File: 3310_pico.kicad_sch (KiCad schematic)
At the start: 37 parts, among them J4 PCDTest, J5 KeypadTest, J6 BuzzerTest, Q1 2N3904, Q2 2N3904, Q3 2N3904

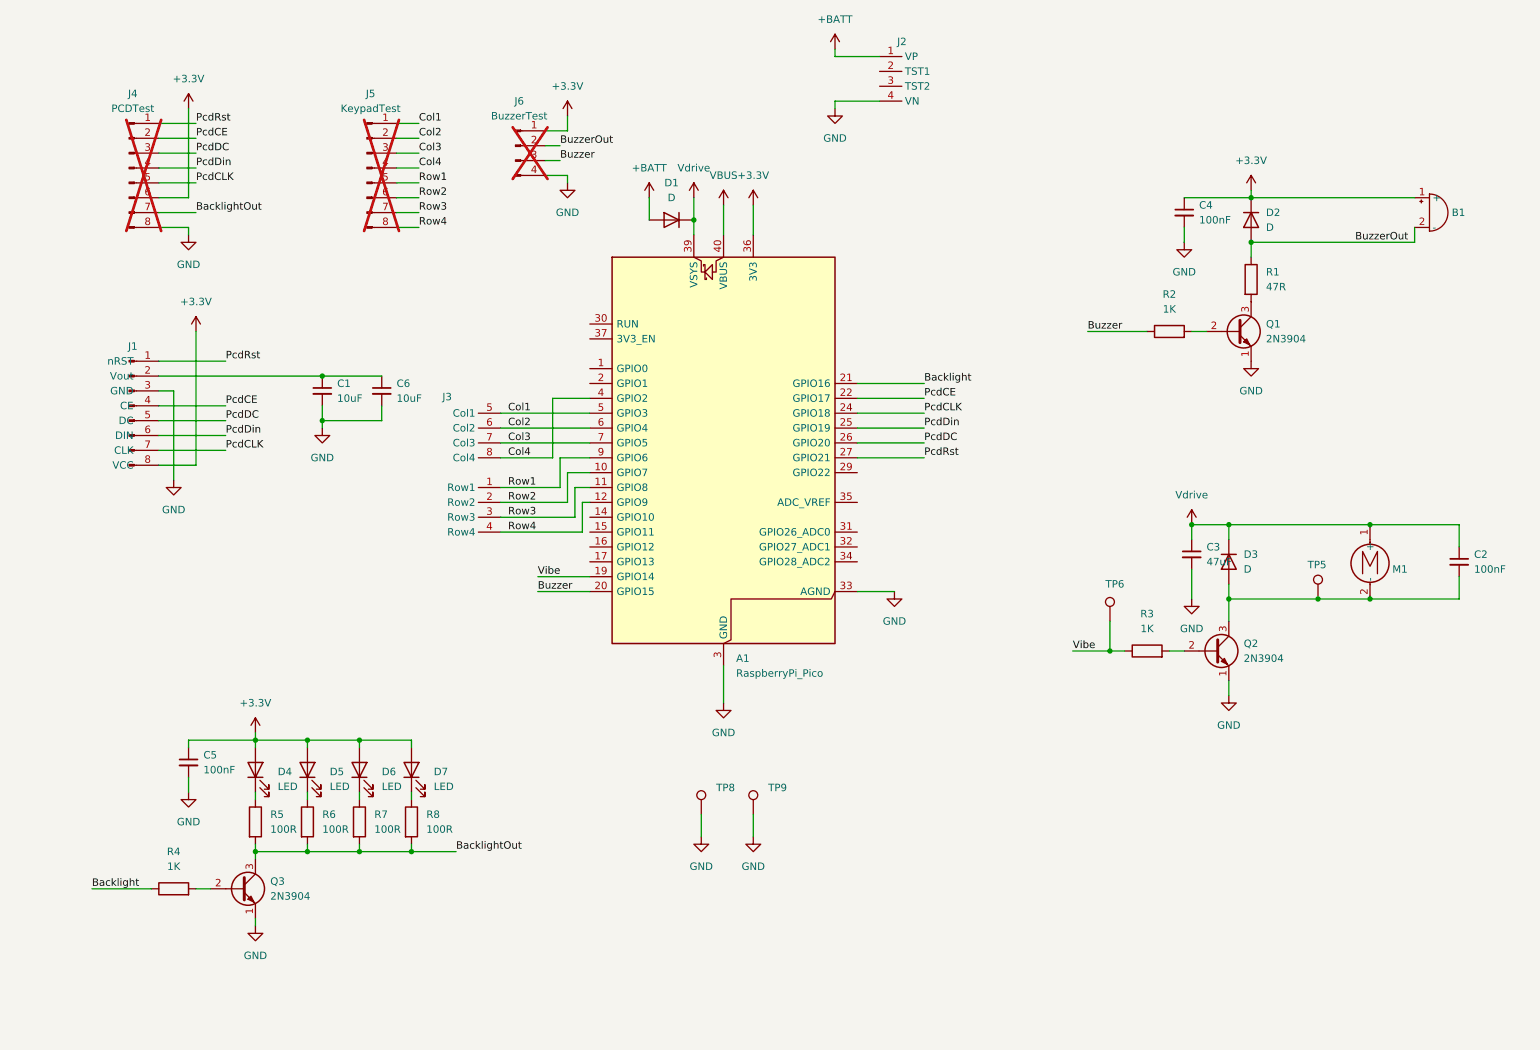
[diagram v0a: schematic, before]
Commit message: Revision 1 with battery charging, rgb backlight, etc
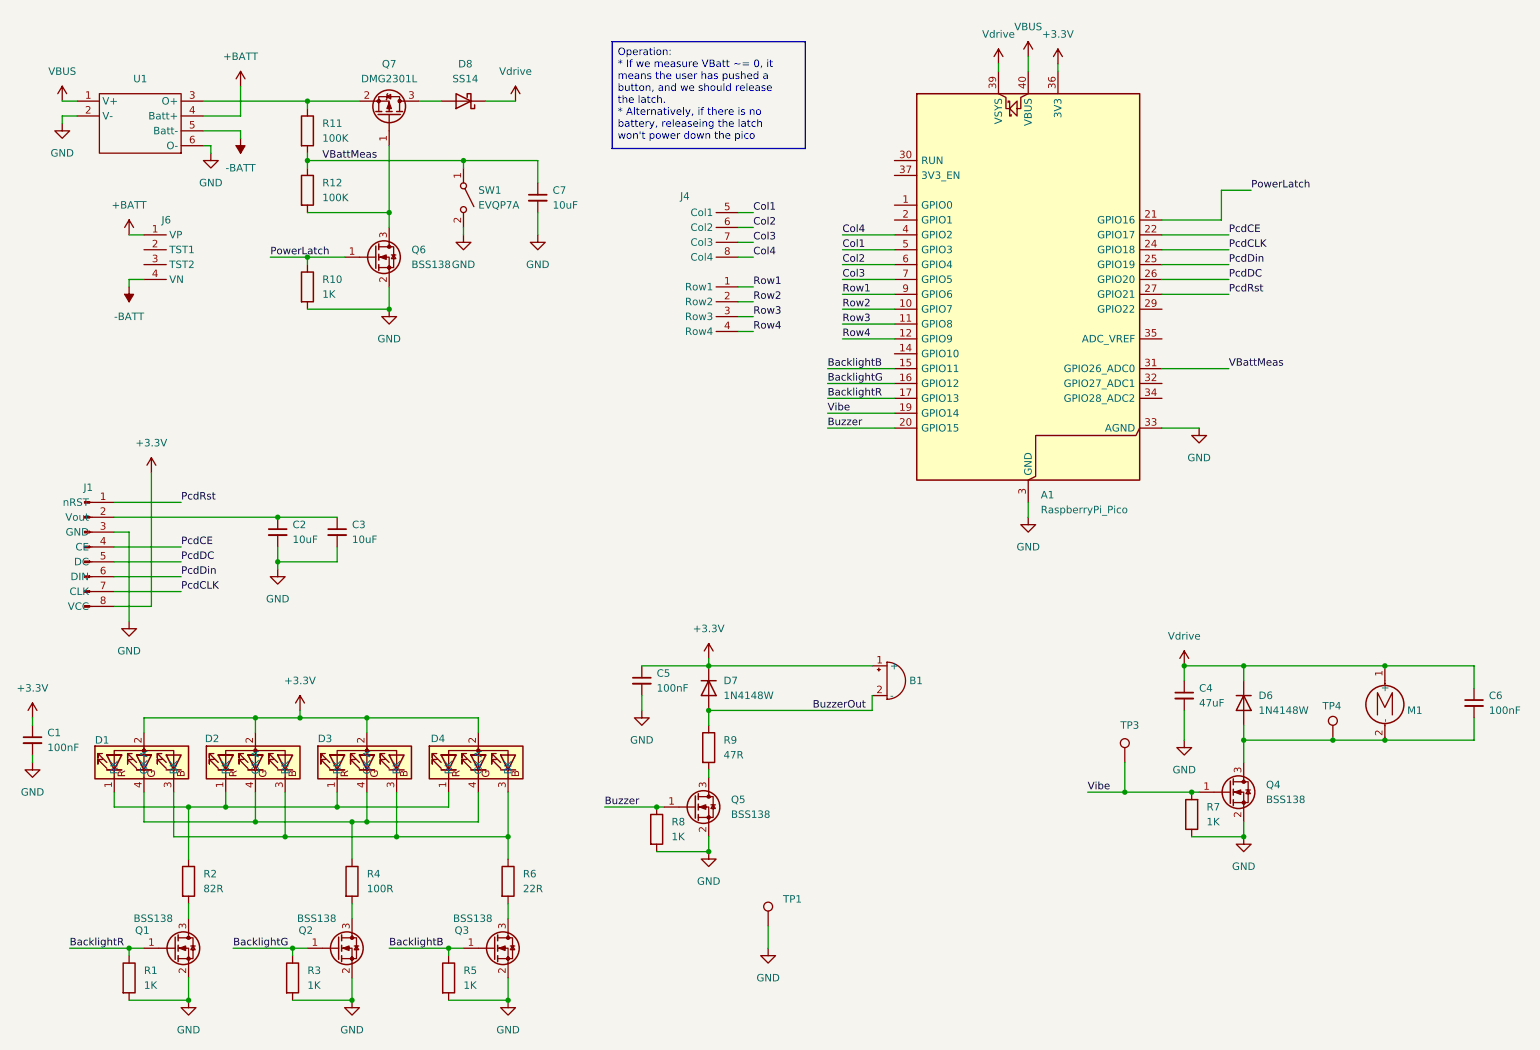
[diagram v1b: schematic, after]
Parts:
- removed D1, D2, D3: D, Diode_THT:D_A-405_P2.54mm_Vertical_AnodeUp, symbol Device:D
- removed D4, D5, D6, D7: LED, 3310Footprints:VoidLED, symbol Device:LED
- removed J4: PCDTest, Connector_PinHeader_2.54mm:PinHeader_1x08_P2.54mm_Vertical, symbol Connector:Conn_01x08_Pin
- removed J5: KeypadTest, Connector_PinHeader_2.54mm:PinHeader_1x08_P2.54mm_Vertical, symbol Connector:Conn_01x08_Pin
- removed J6: BuzzerTest, Connector_PinHeader_2.54mm:PinHeader_1x04_P2.54mm_Vertical, symbol Connector:Conn_01x04_Pin
- removed Q1, Q2, Q3: 2N3904, Package_TO_SOT_THT:TO-92_Inline, symbol Transistor_BJT:2N3904
- removed R8: 100R, Resistor_SMD:R_0805_2012Metric, symbol Device:R
- removed TP9: TestPoint, TestPoint:TestPoint_Pad_D1.0mm, symbol Connector:TestPoint
- added C7: 10uF, Diode_SMD:D_0805_2012Metric, symbol Device:C_Small
- added D1, D2, D3, D4: (no value), 3310Footprints:VoidRGB, symbol 3310conns:QBLP655
- added D6, D7: 1N4148W, Diode_SMD:D_SOD-123, symbol Diode:1N4148W
- added D8: SS14, Diode_SMD:D_SMA, symbol Diode:SS14
- added Q1, Q2, Q3, Q4, Q5, Q6: BSS138, Package_TO_SOT_SMD:SOT-23, symbol Transistor_FET:BSS138
- added Q7: DMG2301L, Package_TO_SOT_SMD:SOT-23, symbol Transistor_FET:DMG2301L
- added R10, R3, R5: 1K, Resistor_SMD:R_0805_2012Metric, symbol Device:R
- added R11, R12: 100K, Resistor_SMD:R_0805_2012Metric, symbol Device:R
- added SW1: EVQP7A, Button_Switch_SMD:SW_SPST_EVQP7A, symbol Switch:SW_SPST
- added U1: (no value), 3310Footprints:TP4056_charger, symbol 3310conns:Charger
- R2: renamed from R5; value 100R -> 82R
- R6: renamed from R7; value 100R -> 22R
- renumbered C5 to C1, C1 to C2, C6 to C3, C3 to C4, C4 to C5, C2 to C6, J3 to J4, J2 to J6, R4 to R1, R6 to R4, R3 to R7, R2 to R8, R1 to R9, TP8 to TP1, TP6 to TP3, TP5 to TP4
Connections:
- net +3.3V: now also D1.2 (A), D2.2 (A), D3.2 (A), D4.2 (A), D7.1 (K)
- net +BATT: now also U1.4 (Batt+)
- net Buzzer: now also Q5.1 (G)
- net BuzzerOut: now also D7.2 (A)
- net GND: now also R1.2, R7.1, R8.2, C7.2, Q1.2 (S), Q2.2 (S), Q3.2 (S), Q4.2 (S), Q5.2 (S), Q6.2 (S), R10.2, R3.2, R5.2, SW1.2 (B), U1.2 (V-), U1.6 (O-); no longer J6.4 (VN)
- net VBUS: now also U1.1 (V+)
- net Vdrive: now also D6.1 (K), D8.1 (K)
- net Vibe: now also R7.2, Q4.1 (G); no longer R7.1
- net at R4.1: now also D1.4 (GK), D2.4 (GK), D3.4 (GK), D4.4 (GK)
- net at R2.1: now also D1.1 (RK), D2.1 (RK), D3.1 (RK), D4.1 (RK)
- net at R6.1: now also D1.3 (BK), D2.3 (BK), D3.3 (BK), D4.3 (BK)
- net at C6.2, M1.2 (-), TP4.1: now also D6.2 (A), Q4.3 (D)
- net at R9.2: now also Q5.3 (D)
- net BacklightB: now reaches A1.15 (GPIO11)
- net BacklightB: now also Q3.1 (G), R5.1
- net BacklightG: now reaches A1.16 (GPIO12)
- net BacklightG: now also Q2.1 (G), R3.1
- net BacklightR: now reaches A1.17 (GPIO13)
- net BacklightR: now also R1.1, Q1.1 (G)
- net VBattMeas: now reaches A1.31 (GPIO26_ADC0)
- net VBattMeas: now also C7.1, R11.2, R12.1, SW1.1 (A)
- net Backlight renamed PowerLatch
- net PowerLatch: now also Q6.1 (G), R10.1; no longer R1.1
- removed net BacklightOut: R2.2, R4.2, R6.2
- new net: Q2.3 (D), R4.2
- new net: Q7.2 (S), R11.1, U1.3 (O+)
- new net: Q3.3 (D), R6.2
- new net: Q1.3 (D), R2.2
- new net: Q6.3 (D), Q7.1 (G), R12.2
- new net: D8.2 (A), Q7.3 (D)
- new net -BATT: J6.4 (VN), U1.5 (Batt-)
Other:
- moved on the sheet: A1, B1, C1, C2, C3, C4, C5, C6, J1, J4, J6, M1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
